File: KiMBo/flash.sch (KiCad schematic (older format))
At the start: 31 parts

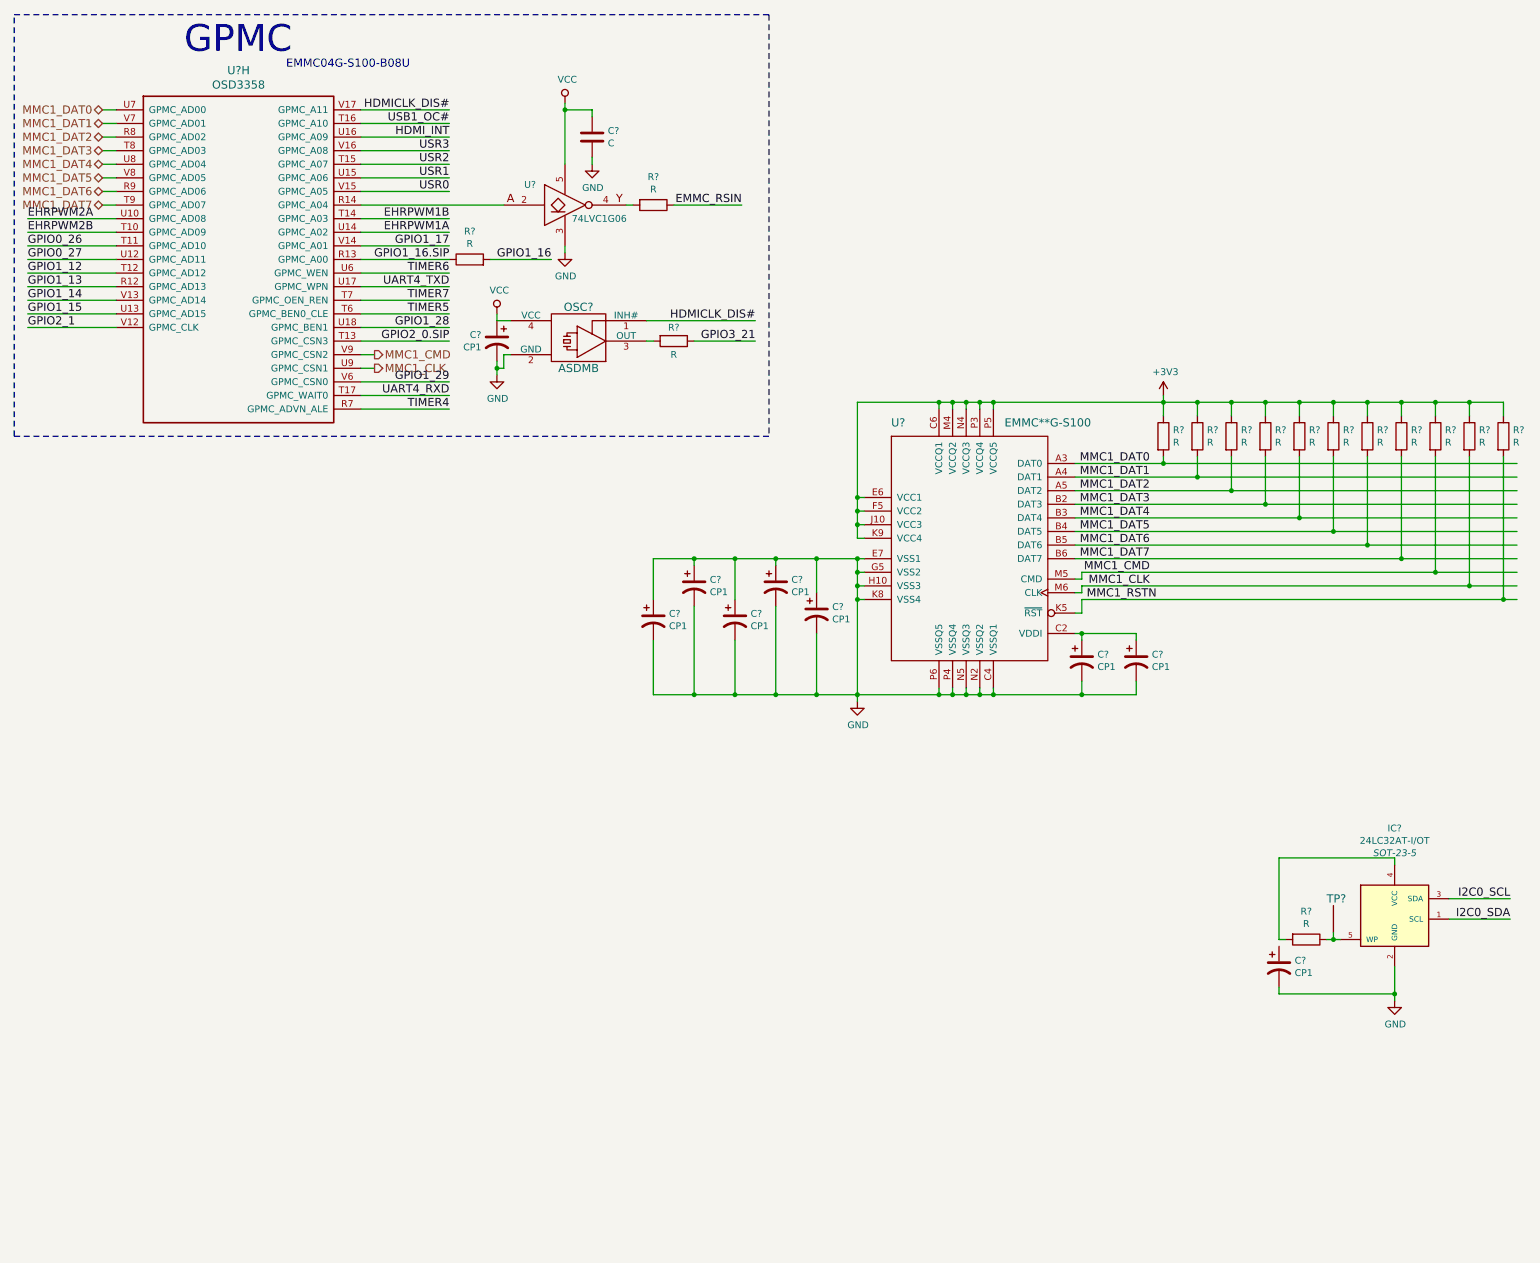
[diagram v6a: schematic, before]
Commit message: Create nodes for more SS, add H stepper, begin fixing power rail names
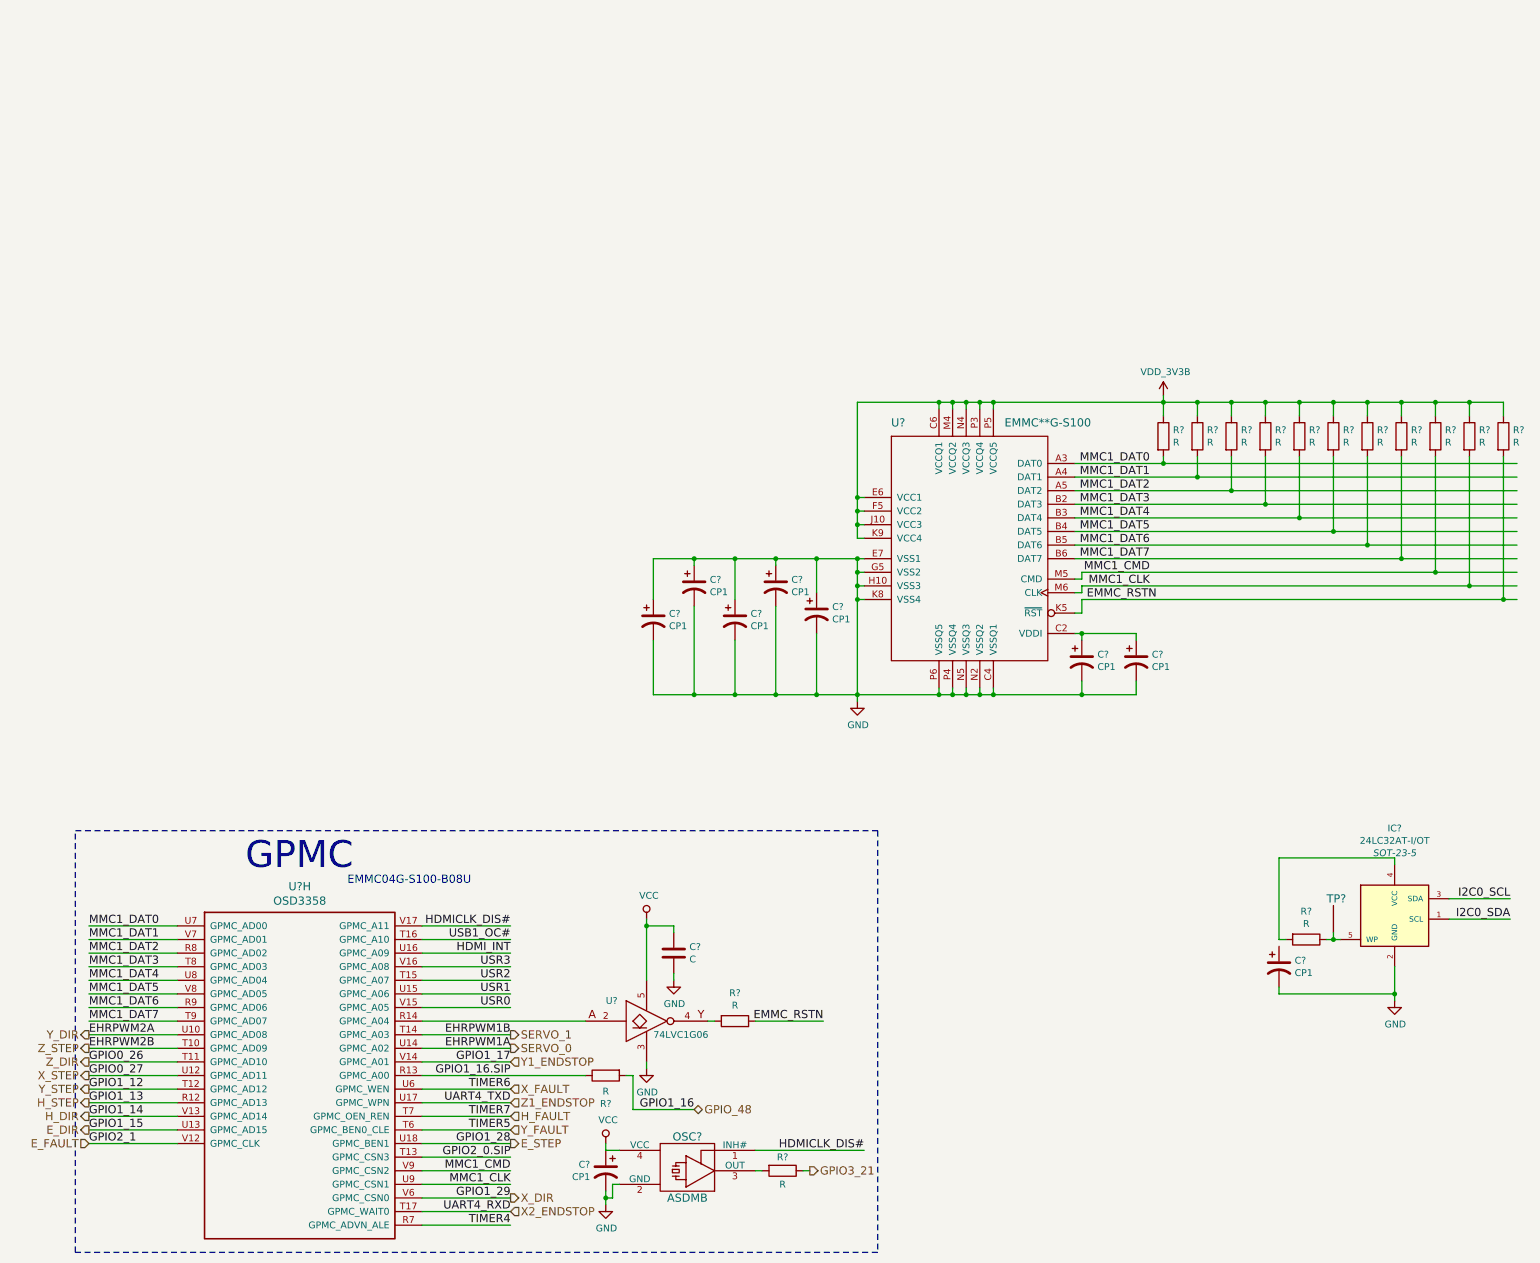
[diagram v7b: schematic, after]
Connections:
- net labels added: EMMC_RSTN, E_DIR, E_FAULT, E_STEP, GPIO_48, H_DIR, H_FAULT, H_STEP, SERVO_0, SERVO_1, VDD_3V3B, X2_ENDSTOP, X_DIR, X_FAULT, X_STEP, Y1_ENDSTOP, Y_DIR, Y_FAULT, Y_STEP, Z1_ENDSTOP, Z_DIR, Z_STEP
- net labels removed: +3V3, EMMC_RSIN, MMC1_RSTN
- wire segments 144 -> 146
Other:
- moved on the sheet: C?, OSC?, R?, U?, U?H

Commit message: Update the rest of the power rails and add two more stepper drivers
Now has *nine* stepper drivers, this will increase cost, and may drastically increase development time...
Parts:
- R?: value R -> 10k
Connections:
- net labels added: ~HDMICLK_DIS, ~USB1_OC
- net labels removed: HDMICLK_DIS#, USB1_OC#, VCC
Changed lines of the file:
@@
 $Descr A3 16535 11693
 encoding utf-8
-Sheet 6 25
+Sheet 6 27
 Title ""
 Date ""
@@
 P 10650 7700
 F 0 "R?" V 10443 7700 50  0000 C CNN
-F 1 "R" V 10534 7700 50  0000 C CNN
+F 1 "10k" V 10534 7700 50  0000 C CNN
 F 2 "" V 10580 7700 50  0000 C CNN
 F 3 "" H 10650 7700 50  0000 C CNN
@@
 	11300 7100 10450 7100
 Wire Wire Line
-	10450 7100 10450 7700
+	10450 7050 10450 7750
 Wire Wire Line
 	10450 7700 10500 7700
@@
 GPIO1_15
 Text Label 4800 7700 2    60   ~ 0
-USB1_OC#
+~USB1_OC
 Text Label 4800 8700 2    60   ~ 0
 GPIO1_16.SIP
@@
 GPIO1_17
 Text Label 4800 7600 2    60   ~ 0
-HDMICLK_DIS#
+~HDMICLK_DIS
 Text Label 4800 7800 2    60   ~ 0
 HDMI_INT
@@
 F 3 "" H 5800 8650 50  0000 C CNN
 	1    5800 8650
-	1    0    0    -1
-$EndComp
-$Comp
-L VCC #PWR?
-U 1 1 58ED63AB
-P 5800 7550
-F 0 "#PWR?" H 5800 7400 50  0001 C CNN
-F 1 "VCC" H 5817 7723 50  0000 C CNN
-F 2 "" H 5800 7550 50  0000 C CNN
-F 3 "" H 5800 7550 50  0000 C CNN
-	1    5800 7550
 	1    0    0    -1
 $EndComp
@@
 $EndComp
 $Comp
-L VCC #PWR?
-U 1 1 58ED63DA
-P 5500 9200
-F 0 "#PWR?" H 5500 9050 50  0001 C CNN
-F 1 "VCC" H 5517 9373 50  0000 C CNN
-F 2 "" H 5500 9200 50  0000 C CNN
-F 3 "" H 5500 9200 50  0000 C CNN
-	1    5500 9200
-	1    0    0    -1
-$EndComp
-$Comp
 L R R?
 U 1 1 58ED63E0
@@
 $EndComp
 Text Label 7400 9250 2    60   ~ 0
-HDMICLK_DIS#
+~HDMICLK_DIS
 Wire Wire Line
 	4800 8100 4150 8100
@@
 	1    0    0    -1
 $EndComp
+Text HLabel 4800 7900 2    60   Output ~ 0
+USR3
+Text HLabel 4800 8000 2    60   Output ~ 0
+USR2
+Text HLabel 4800 8100 2    60   Output ~ 0
+USR1
+Text HLabel 4800 8200 2    60   Output ~ 0
+USR0
+$Comp
+L VDD_3V3B #PWR?
+U 1 1 59FAFB00
+P 5500 9200
+F 0 "#PWR?" H 5500 9050 50  0001 C CNN
+F 1 "VDD_3V3B" H 5515 9373 50  0000 C CNN
+F 2 "" H 5500 9200 50  0000 C CNN
+F 3 "" H 5500 9200 50  0000 C CNN
+	1    5500 9200
+	1    0    0    -1
+$EndComp
+$Comp
+L VDD_3V3B #PWR?
+U 1 1 59FBC4DE
+P 5800 7550
+F 0 "#PWR?" H 5800 7400 50  0001 C CNN
+F 1 "VDD_3V3B" H 5815 7723 50  0000 C CNN
+F 2 "" H 5800 7550 50  0000 C CNN
+F 3 "" H 5800 7550 50  0000 C CNN
+	1    5800 7550
+	1    0    0    -1
+$EndComp
+Connection ~ 10450 7700
+$Comp
+L VDD_3V3B #PWR?
+U 1 1 59FBD7EE
+P 10450 7050
+F 0 "#PWR?" H 10450 6900 50  0001 C CNN
+F 1 "VDD_3V3B" H 10465 7223 50  0000 C CNN
+F 2 "" H 10450 7050 50  0000 C CNN
+F 3 "" H 10450 7050 50  0000 C CNN
+	1    10450 7050
+	1    0    0    -1
+$EndComp
+Connection ~ 10450 7100
 $EndSCHEMATC
